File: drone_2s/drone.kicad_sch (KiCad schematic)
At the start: 45 parts, among them J1 Conn_01x06, J2 Conn_01x02, J3 Conn_01x02, J4 Conn_01x02, J5 Conn_01x02, J6 Conn_01x02, Q1 Si2319CDS, Q2 Si2319CDS, Q3 Si2319CDS, Q4 Si2319CDS, SW1 SW_Push_Open, SW2 SW_Push_Open, U1 ESP32-WROOM-32, U2 MPU-6050, U3 DWM1000, U4 BMP280, U5 LM1117MP-3.3

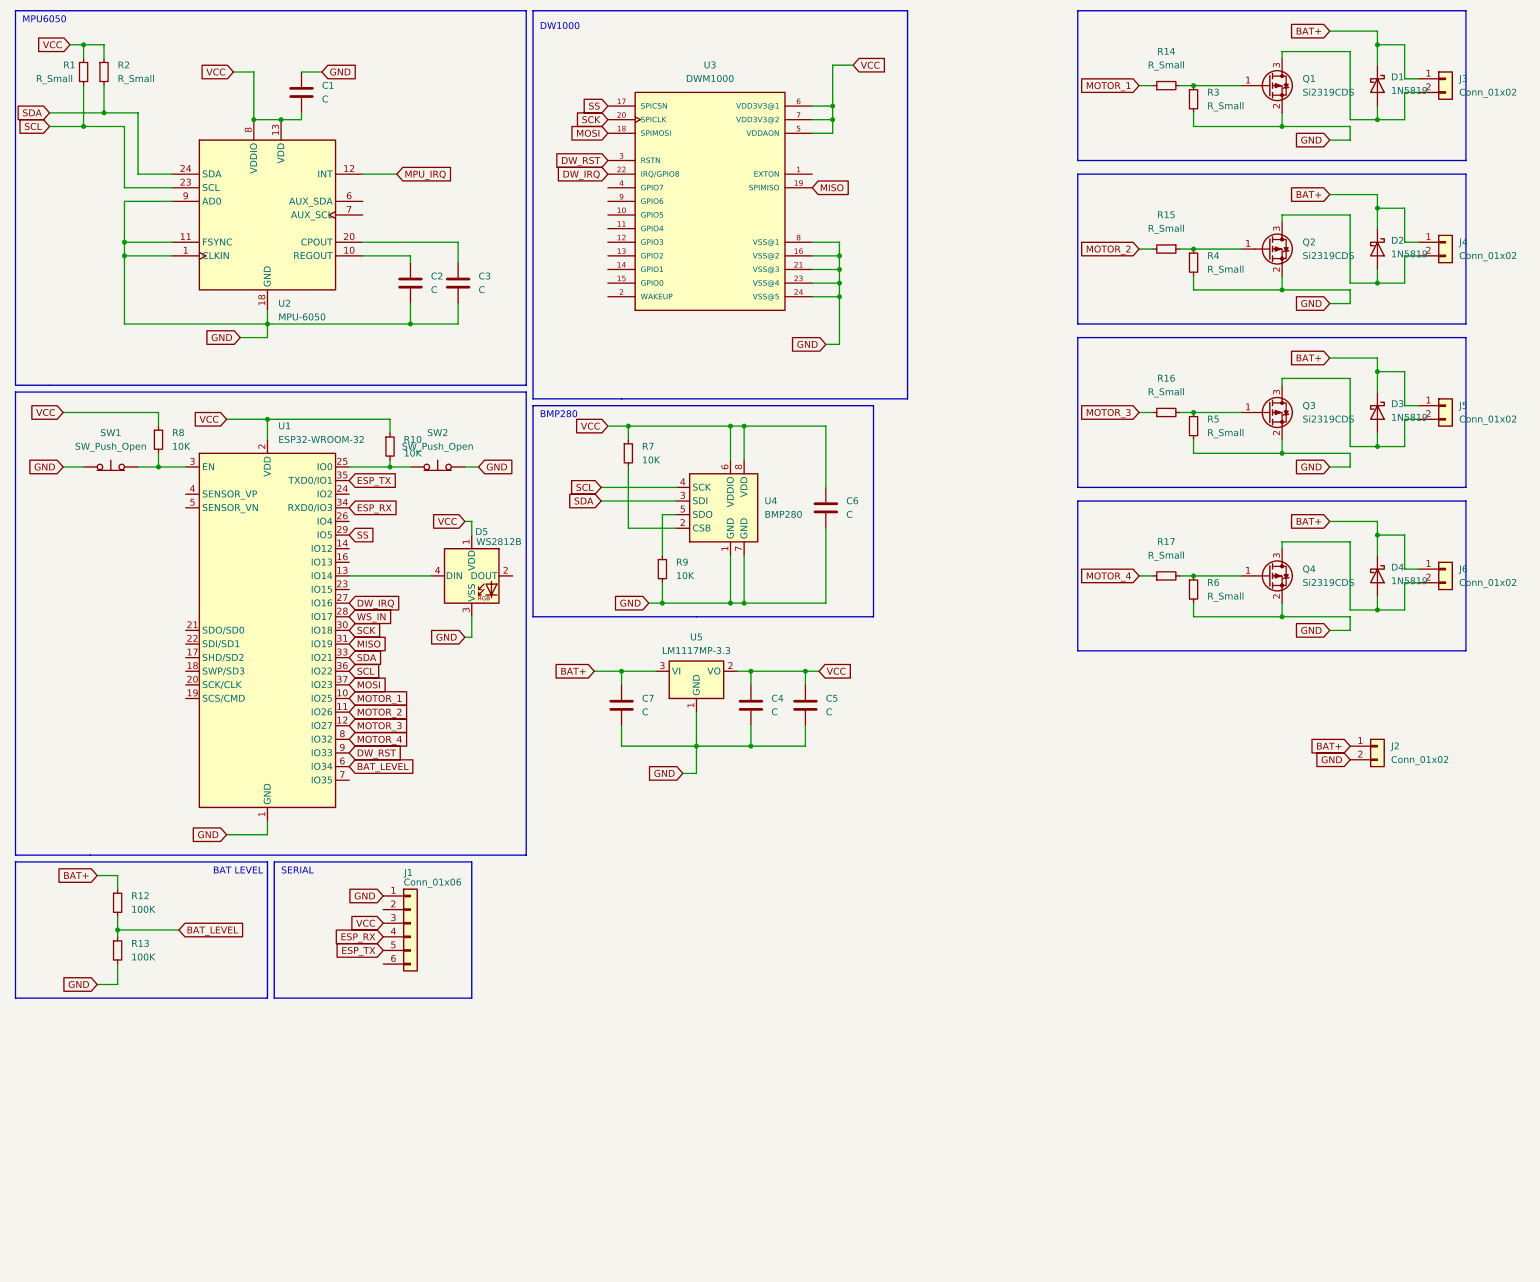
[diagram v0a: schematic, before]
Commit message: motors mounted on pcb + usb program
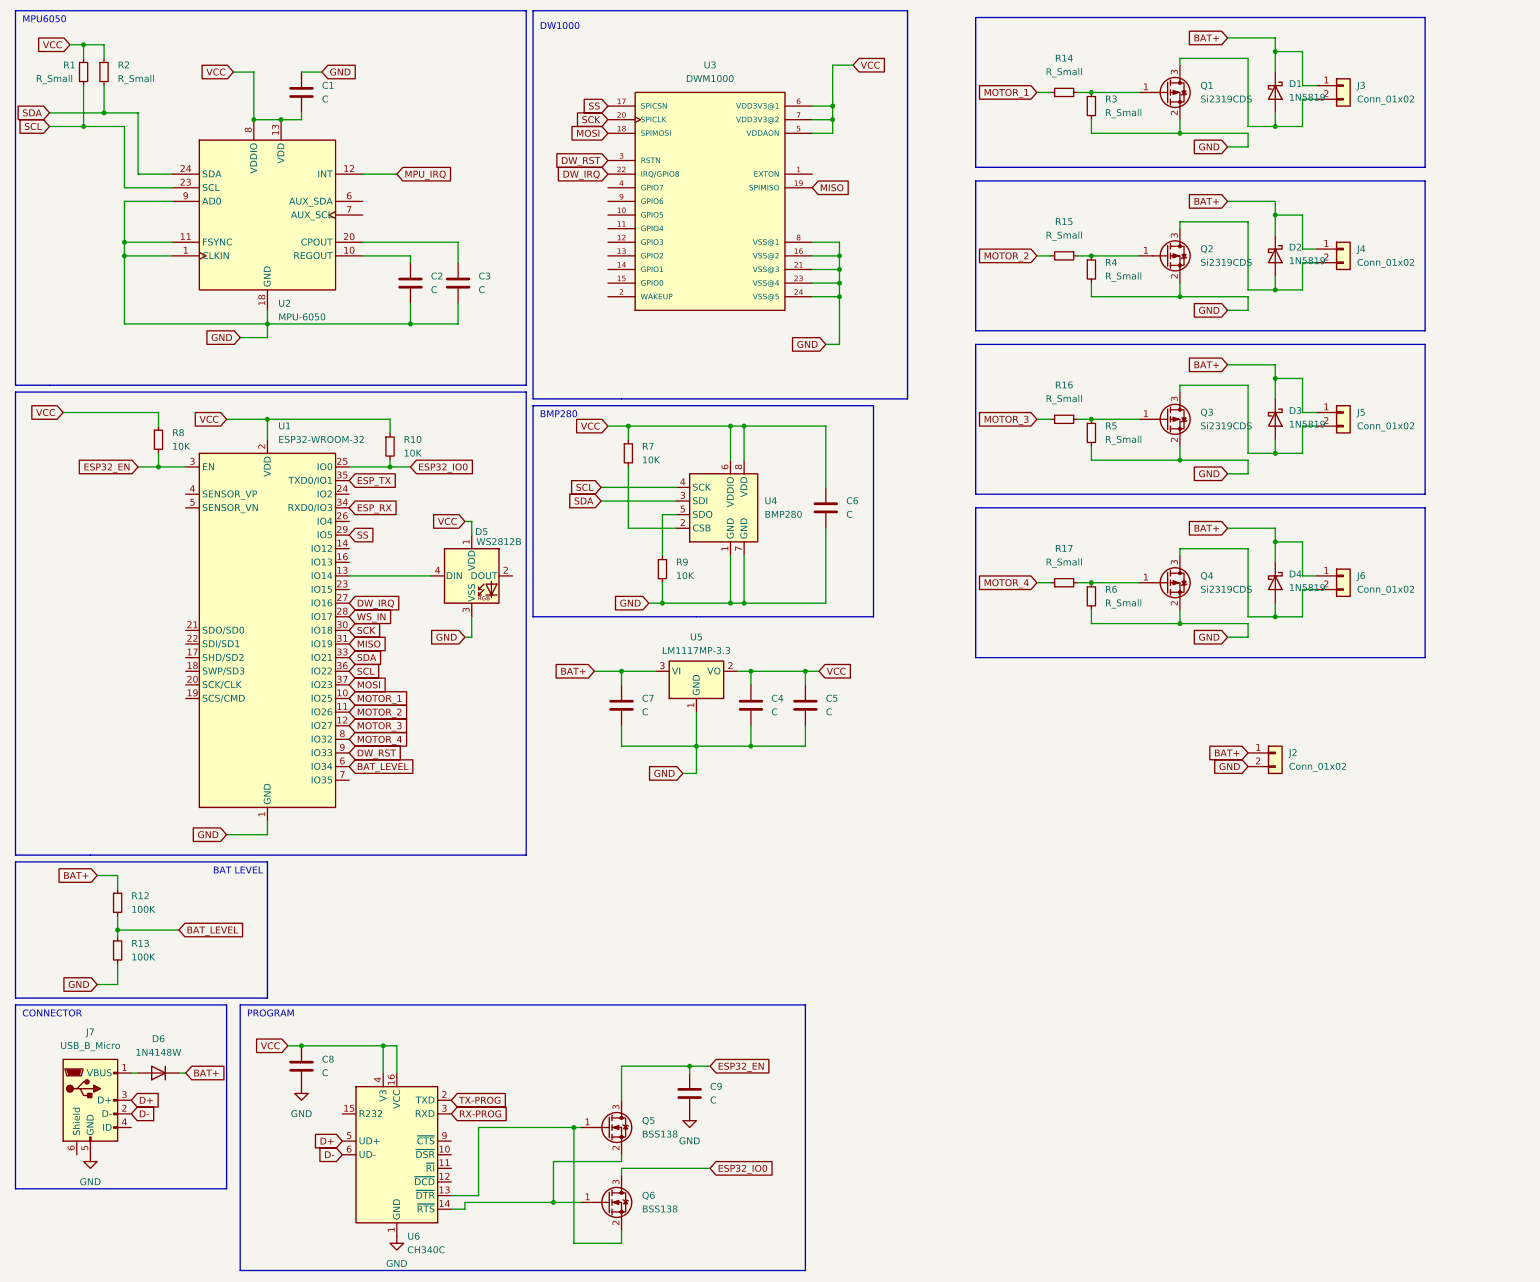
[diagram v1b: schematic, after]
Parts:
- removed J1: Conn_01x06, Connector_PinHeader_2.54mm:PinHeader_1x06_P2.54mm_Vertical, symbol Connector_Generic:Conn_01x06
- removed SW1, SW2: SW_Push_Open, Button_Switch_SMD:SW_SPST_CK_RS282G05A3, symbol Switch:SW_Push_Open
- added C8, C9: C, Capacitor_SMD:C_0603_1608Metric, symbol Device:C
- added D6: 1N4148W, Diode_SMD:D_SOD-123, symbol Diode:1N4148W
- added J7: USB_B_Micro, Connector_USB:USB_Micro-B_Amphenol_10118194_Horizontal, symbol Connector:USB_B_Micro
- added Q5, Q6: BSS138, Package_TO_SOT_SMD:SOT-23, symbol Transistor_FET:BSS138
- added U6: CH340C, Package_SO:SOIC-16_3.9x9.9mm_P1.27mm, symbol Interface_USB:CH340C
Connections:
- net BAT+: now also D6.1 (K)
- net GND: now also C8.2, C9.2, J7.5 (GND), U6.1 (GND)
- net VCC: now also C8.1, U6.16 (VCC), U6.4 (V3)
- net ESP32_IO0: now reaches R10.2, U1.25 (IO0)
- net ESP32_IO0: now also Q6.3 (D)
- net ESP32_EN: now reaches R8.2, U1.3 (EN)
- net ESP32_EN: now also C9.1, Q5.3 (D)
- new net: D6.2 (A), J7.1 (VBUS)
- new net: Q5.2 (S), Q6.1 (G), U6.14 (~{RTS})
- new net: Q5.1 (G), Q6.2 (S), U6.13 (~{DTR})
- new net D+: J7.3 (D+), U6.5 (UD+)
- new net D-: J7.2 (D-), U6.6 (UD-)
- new net RX-PROG: U6.3 (RXD)
- new net TX-PROG: U6.2 (TXD)
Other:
- note added: "CONNECTOR"
- note added: "PROGRAM"
- note removed: "SERIAL"
- moved on the sheet: D1, D2, D3, D4, J2, J3, J4, J5, J6, Q1, Q2, Q3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

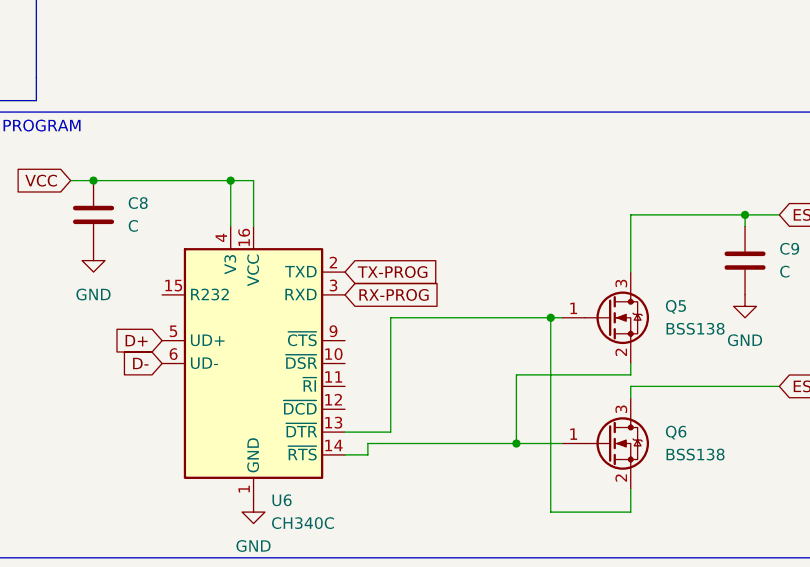
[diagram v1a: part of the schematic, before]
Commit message: fix drone uart wiring
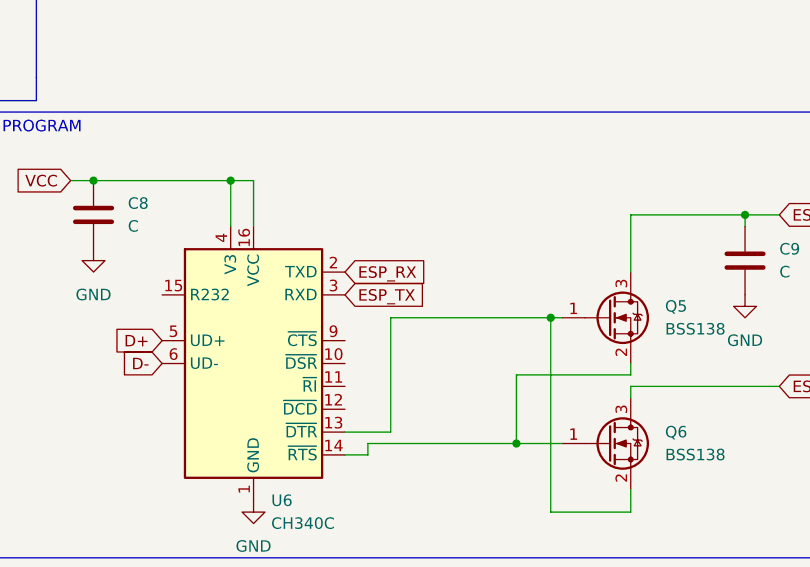
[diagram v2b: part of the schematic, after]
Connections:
- net RX-PROG is gone; now on net ESP_TX: U6.3 (RXD)
- net TX-PROG is gone; now on net ESP_RX: U6.2 (TXD)
